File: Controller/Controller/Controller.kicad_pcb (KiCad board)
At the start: 2 copper layers, 125 parts, among them J1 Conn_01x01_Pin, J10 Conn_01x01_Pin, J11 Conn_02x05_Odd_Even, J2 Conn_01x01_Pin, J3 Conn_01x01_Pin, J4 Conn_01x01_Pin, J5 Conn_01x01_Pin, J6 Conn_01x01_Pin, J7 Conn_01x01_Pin, J8 Conn_01x01_Pin, J9 Conn_01x01_Pin, Q1 2N3906, Q2 2N5457, Q3 2N5457, U1 TL071, U2 TL072, U3 LF444, U4 TL074, U5 TL074, U6 TL072

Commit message: controller almost routed
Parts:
- added J12: Conn_01x01_Pin, Connector_Pin:Pin_D1.0mm_L10.0mm, F.Cu at (37.6, 149.9)
- added J13: Conn_01x01_Pin, Connector_Pin:Pin_D1.0mm_L10.0mm, F.Cu at (147.8, 146.6)
- C3: renamed from C24; value 100nF -> 4.7nF
- D1: renamed from D5; footprint Diode_THT:D_DO-35_SOD27_P7.62mm_Horizontal -> Diode_THT:D_T-1_P5.08mm_Horizontal
- D10, D11, D4, D6, D7: footprint Diode_THT:D_DO-35_SOD27_P7.62mm_Horizontal -> Diode_THT:D_T-1_P5.08mm_Horizontal
- D2: renamed from D1; footprint Diode_THT:D_DO-35_SOD27_P7.62mm_Horizontal -> Diode_THT:D_T-1_P5.08mm_Horizontal
- D3: renamed from D2; footprint Diode_THT:D_DO-35_SOD27_P7.62mm_Horizontal -> Diode_THT:D_T-1_P5.08mm_Horizontal
- D5: renamed from D3; footprint Diode_THT:D_DO-35_SOD27_P7.62mm_Horizontal -> Diode_THT:D_T-1_P5.08mm_Horizontal
- D8: renamed from D9; footprint Diode_THT:D_DO-35_SOD27_P7.62mm_Horizontal -> Diode_THT:D_T-1_P5.08mm_Horizontal
- D9: renamed from D8; footprint Diode_THT:D_DO-35_SOD27_P7.62mm_Horizontal -> Diode_THT:D_T-1_P5.08mm_Horizontal
- R11: renamed from R53; value 1M -> 100K
- R15: renamed from R46; value 10k -> 100k
- R6: renamed from R51; value 1M -> 300K
- R9: renamed from R52; value 1M -> 100K
- moved C17 208.0 mm to (42.7, 128.2), turned to 90 degrees
- moved C22 207.2 mm to (50.3, 144.0), turned to 90 degrees
- moved C21 186.7 mm to (63.5, 128.3), turned to 90 degrees
- moved C14 184.6 mm to (63.0, 144.0), turned to 90 degrees
- moved C16 174.7 mm to (85.1, 144.0), turned to 90 degrees
- moved C19 165.5 mm to (85.1, 128.0), turned to 90 degrees
- moved C18 154.2 mm to (105.4, 144.0), turned to 90 degrees
- moved C15 153.7 mm to (97.8, 128.2), turned to 90 degrees
- moved C4 153.1 mm to (42.2, 146.8), turned to 90 degrees
- moved C1 137.0 mm to (53.1, 139.7), turned to 90 degrees
- moved C5 130.3 mm to (60.5, 146.8)
- moved C12 129.2 mm to (120.9, 144.0), turned to 90 degrees
- moved C2 127.8 mm to (58.4, 128.3), turned to 180 degrees
- moved R5 127.5 mm to (44.5, 146.8), turned to 90 degrees
- moved C11 124.3 mm to (120.9, 128.2), turned to 90 degrees
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- renumbered C20 to C1, C19 to C10, C3 to C11, C1 to C12, C4 to C13, C2 to C14, C5 to C15, C10 to C16, C6 to C17, C11 to C18, C7 to C19, C21 to C2, C12 to C20, C8 to C21, C13 to C22, C9 to C23, C14 to C24, C15 to C25, C16 to C26, C17 to C4, C22 to C5, C25 to C6, C26 to C7, C23 to C8, C18 to C9, J11 to J1, J9 to J10, J10 to J11, J1 to J2, J2 to J3, J3 to J4, J4 to J5, J5 to J6, J6 to J7, J7 to J8, J8 to J9, Q3 to Q1, Q1 to Q3, R38 to R1, R42 to R10, R44 to R12, R45 to R13, R54 to R14, R47 to R16, R55 to R17, R49 to R18, R48 to R19, R39 to R2, R37 to R20, R35 to R21, R36 to R22, R57 to R23, R56 to R24, R59 to R25, R58 to R26, R60 to R27, R61 to R28, R1 to R29, R50 to R3, R10 to R30, R19 to R31, R2 to R32, R11 to R33, R20 to R34, R3 to R35, R12 to R36, R21 to R37, R4 to R38, R13 to R39, R40 to R4, R22 to R40, R5 to R41, R14 to R42, R23 to R43, R6 to R44, R15 to R45, R24 to R46, R7 to R47, R16 to R48, R25 to R49, R34 to R5, R8 to R50, R17 to R51, R26 to R52, R9 to R53, R18 to R54, R27 to R55, R28 to R56, R29 to R57, R30 to R58, R31 to R59, R32 to R60, R33 to R61, R41 to R7, R43 to R8, U5 to U1, U4 to U2, U2 to U3, U3 to U4, U6 to U5, U1 to U6
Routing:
- net -12V: track 6.86 -> 205.4 mm, vias 0 -> 1
- net +12V: track 6.86 -> 187.0 mm
- net TLA: track 0.00 -> 96.2 mm
- net GLA: track 0.00 -> 86.0 mm
- net Net-(Q2-S): track 0.00 -> 78.5 mm
- net ISRC: track 2.00 -> 62.0 mm
- net Net-(U1B--): track 0.00 -> 42.2 mm
- net CV2: track 0.00 -> 39.6 mm
- net Net-(D6-K): track 0.00 -> 27.9 mm
- net KBUS: track 0.00 -> 27.0 mm
- net Net-(Q3-E): track 0.00 -> 26.6 mm
- net Net-(D4-K): track 0.00 -> 25.8 mm
- net Net-(U2B-+): track 0.00 -> 22.5 mm
- net CV1: track 0.00 -> 20.3 mm
- net Net-(Q3-B): track 0.00 -> 19.7 mm
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- added copper zone on B.Cu, net GND

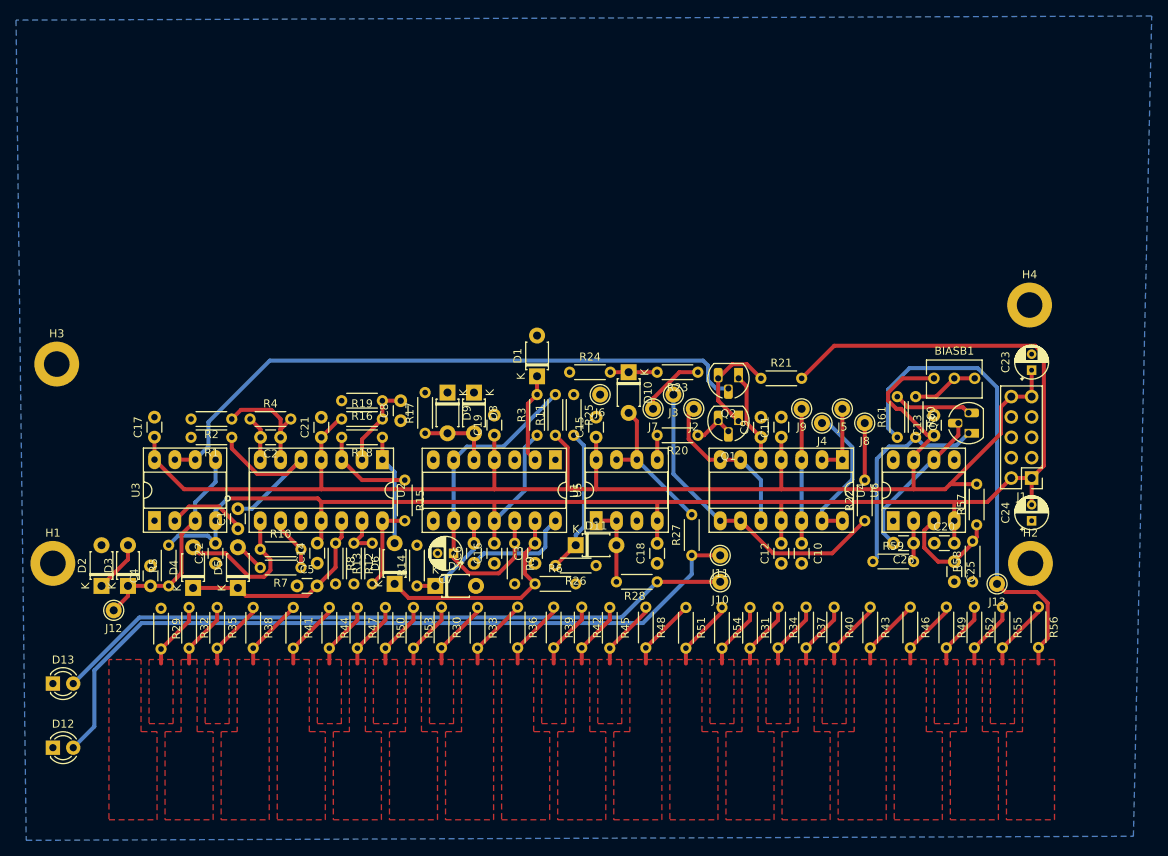
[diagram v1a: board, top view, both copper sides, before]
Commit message: controller routed
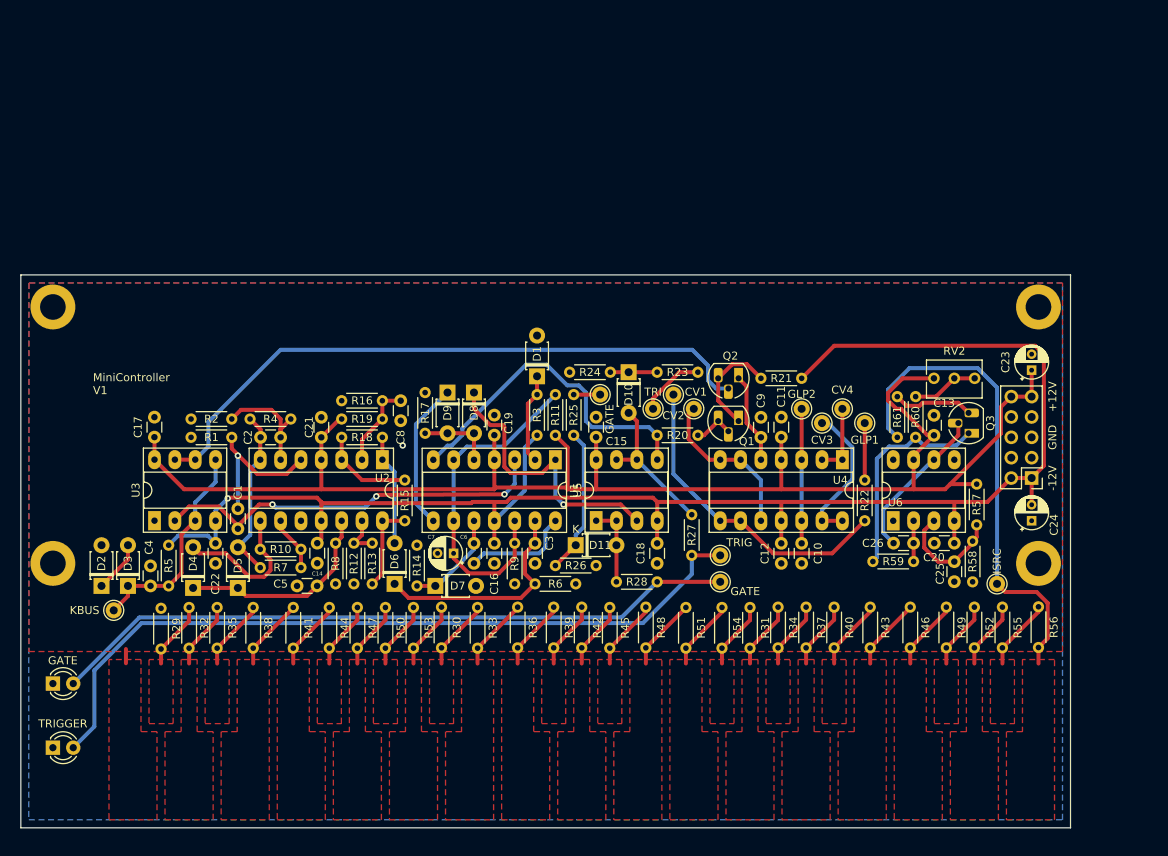
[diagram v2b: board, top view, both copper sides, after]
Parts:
- moved H3 7.14 mm to (30.0, 112.0)
- moved H4 1.13 mm to (153.0, 112.0)
- moved H2 1.00 mm to (153.0, 144.0)
- renumbered BIASB1 to RV2
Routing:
- net Net-(U1A-+): track 9.97 -> 50.4 mm, vias 0 -> 3
- net Net-(U5B-+): track 3.04 -> 42.1 mm
- net Net-(D8-K): track 0.00 -> 35.1 mm, vias 0 -> 1
- net Net-(D9-K): track 0.00 -> 18.5 mm
- net Net-(D5-A): track 9.49 -> 21.6 mm
- net Net-(U2B-+): track 22.5 -> 18.8 mm, vias 0 -> 1
- net GATE: track 0.00 -> 3.30 mm
- net GND: track 0.00 -> 1.78 mm, vias 0 -> 1
- net Net-(Q2-S): track 78.5 -> 79.6 mm
- net -12V: track 205.4 -> 206.1 mm
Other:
- board outline added: 131 x 69 mm
- board text added: "+12V"
- board text added: "-12V"
- board text added: "CV1"
- board text added: "CV2"
- board text added: "CV3"
- board text added: "CV4"
- board text added: "GATE"
- board text added: "GLP1"
- board text added: "GLP2"
- board text added: "GND"
- board text added: "ISRC"
- board text added: "KBUS"
- board text added: "MiniController V1"
- board text added: "TRI"
- board text added: "TRIG"
- board text added: "TRIGGER"

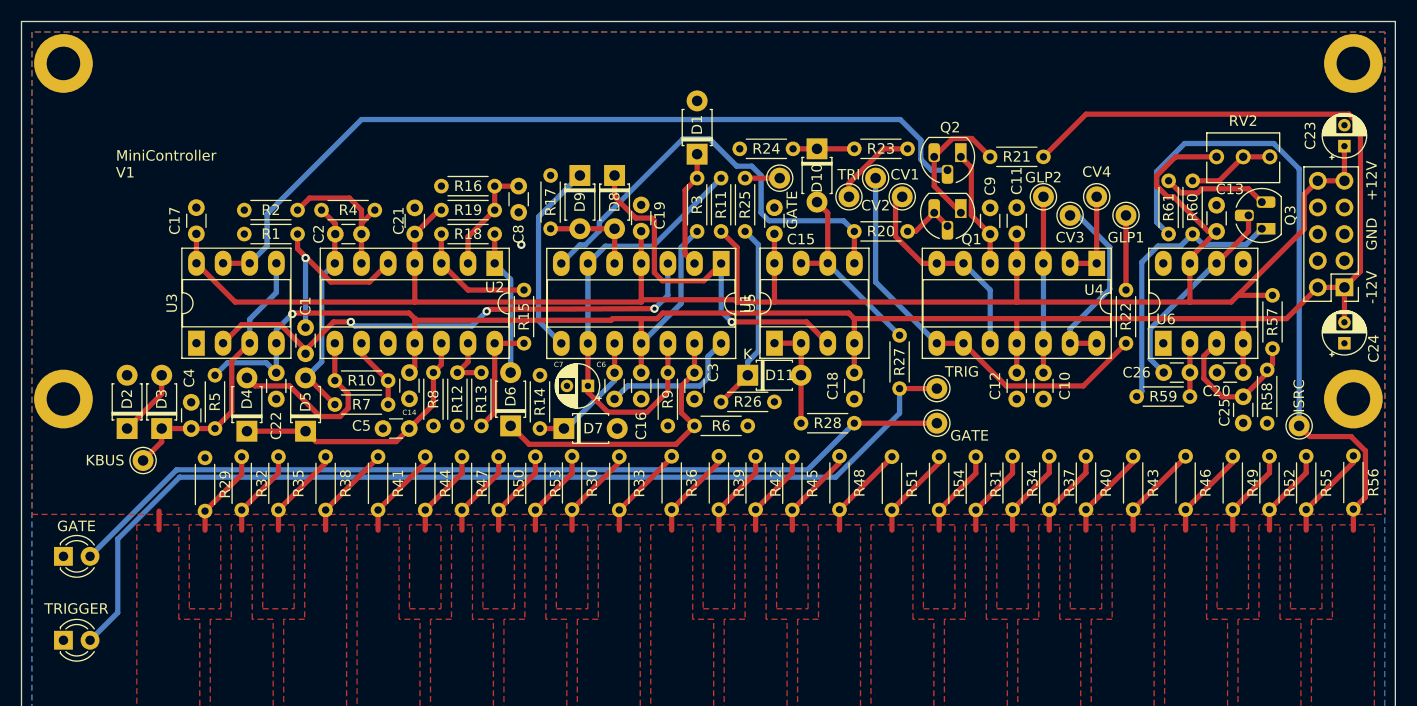
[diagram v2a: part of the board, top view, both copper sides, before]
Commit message: controller - changed resistor sizes
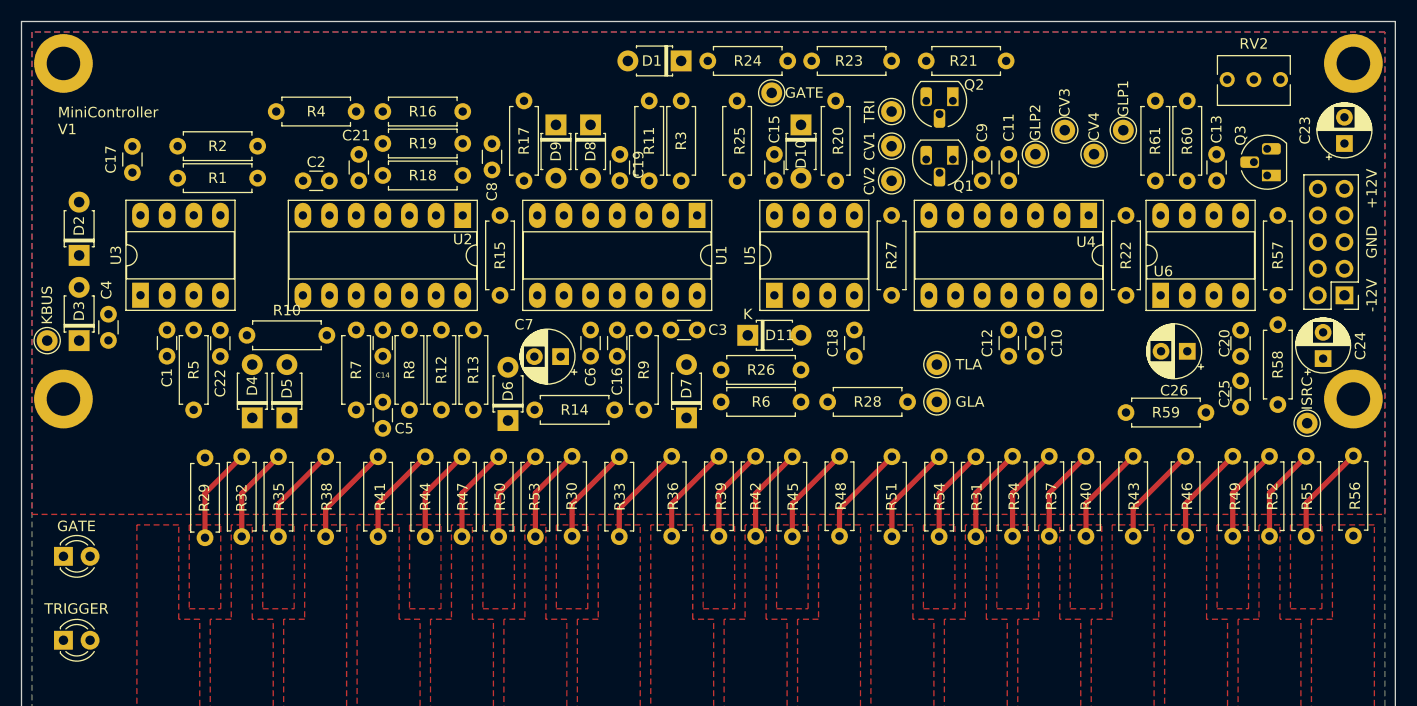
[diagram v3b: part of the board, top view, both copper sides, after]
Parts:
- C23, C24, C7: footprint Capacitor_THT:CP_Radial_D4.0mm_P2.00mm -> Capacitor_THT:CP_Radial_D5.0mm_P2.50mm
- C26: footprint Capacitor_THT:C_Disc_D3.0mm_W1.6mm_P2.50mm -> Capacitor_THT:CP_Radial_D5.0mm_P2.50mm
- R1, R10, R11, R12, R13, R14, R15, R16, R17, R18, R19, R2, R20, R21, R22, R23, R24, R25, R26, R27, R28, R29, R3, R30, R31, R32, R33, R34, R35, R36, R37, R38, R39, R4, R40, R41, R42, R43, R44, R45, R46, R47, R48, R49, R5, R50, R51, R52, R53, R54, R55, R56, R57, R58, R59, R6, R60, R61, R7, R8, R9: footprint Resistor_THT:R_Axial_DIN0204_L3.6mm_D1.6mm_P5.08mm_Horizontal -> Resistor_THT:R_Axial_DIN0207_L6.3mm_D2.5mm_P7.62mm_Horizontal
- moved D2 17.1 mm to (31.5, 130.3)
- moved J12 14.6 mm to (28.4, 138.4)
- moved R20 14.2 mm to (103.6, 115.6), turned to -90 degrees
- moved C1 13.4 mm to (39.9, 137.4), turned to -90 degrees
- moved D7 11.7 mm to (89.4, 145.8), turned to 90 degrees
- moved C4 11.5 mm to (34.3, 138.4)
- moved D3 11.5 mm to (31.5, 138.4)
- moved R21 11.0 mm to (112.3, 111.8)
- moved R4 10.3 mm to (50.3, 116.6)
- moved R5 9.62 mm to (42.4, 137.4), turned to -90 degrees
- moved R10 9.43 mm to (47.5, 137.9)
- moved R13 9.18 mm to (69.1, 137.4), turned to -90 degrees
- moved J7 9.09 mm to (109.0, 116.6)
- moved D1 9.02 mm to (88.9, 111.8), turned to 180 degrees
- moved R27 8.92 mm to (109.0, 134.1)
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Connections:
- net TRI renamed TRIG
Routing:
- net -12V: track 206.1 -> 0.00 mm, vias 1 -> 0
- net +12V: track 187.1 -> 0.00 mm
- net TLA: track 96.2 -> 0.00 mm
- net GLA: track 86.0 -> 0.00 mm
- net Net-(Q2-S): track 79.6 -> 0.00 mm
- net ISRC: track 62.0 -> 0.00 mm
- net Net-(U1A-+): track 50.4 -> 0.00 mm, vias 3 -> 0
- net Net-(U1B--): track 42.1 -> 0.00 mm
- net Net-(U5B-+): track 42.1 -> 0.00 mm
- net CV2: track 39.6 -> 0.00 mm
- net Net-(D8-K): track 35.1 -> 0.00 mm, vias 1 -> 0
- net Net-(D6-K): track 27.9 -> 0.00 mm
- net KBUS: track 27.0 -> 0.00 mm
- net Net-(Q3-E): track 26.6 -> 0.00 mm
- net Net-(D4-K): track 25.8 -> 0.00 mm
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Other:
- board text added: "GLA"
- board text added: "TLA"
- board text removed: "TRIG"

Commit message: controller routed with correct resistor sizes
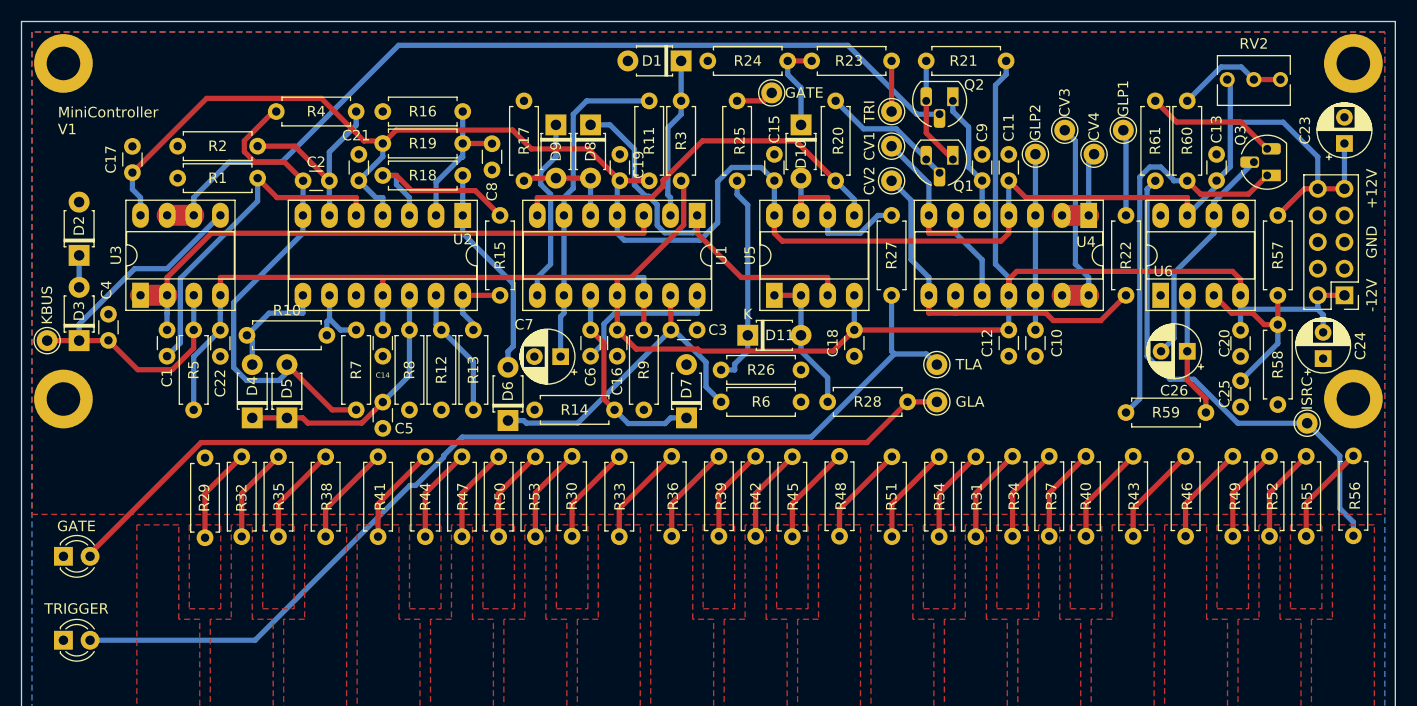
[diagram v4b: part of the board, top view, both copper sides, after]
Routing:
- net +12V: track 0.00 -> 187.8 mm
- net -12V: track 0.00 -> 186.0 mm
- net TLA: track 0.00 -> 98.3 mm
- net GLA: track 0.00 -> 87.0 mm
- net Net-(Q2-S): track 0.00 -> 84.1 mm
- net Net-(U1A-+): track 0.00 -> 56.5 mm
- net Net-(D5-A): track 0.00 -> 48.7 mm
- net ISRC: track 0.00 -> 47.5 mm
- net Net-(U1B--): track 0.00 -> 44.0 mm
- net KBUS: track 0.00 -> 40.4 mm
- net Net-(U5B-+): track 0.00 -> 38.3 mm
- net Net-(Q3-E): track 0.00 -> 37.4 mm
- net Net-(D8-K): track 0.00 -> 36.6 mm
- net CV2: track 0.00 -> 35.9 mm
- net Net-(U2B-+): track 0.00 -> 32.4 mm
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
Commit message: Controller - minor clean up
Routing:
- net Net-(D10-A): track 18.0 -> 13.6 mm
- net CV1: track 22.7 -> 19.3 mm
- net Net-(U2A-+): track 18.4 -> 15.2 mm
- net Net-(U2B-+): track 32.4 -> 31.4 mm
- net Net-(D8-K): track 36.6 -> 35.6 mm
- net GND: vias 0 -> 1
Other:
- board text added: "JLCJLCJLCJLC"

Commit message: minor cleanup
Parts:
- R1, R10, R11, R12, R13, R14, R15, R16, R17, R18, R19, R2, R20, R21, R22, R23, R24, R25, R26, R27, R28, R29, R3, R30, R31, R32, R33, R34, R35, R36, R37, R38, R39, R4, R40, R41, R42, R43, R44, R45, R46, R47, R48, R49, R5, R50, R51, R52, R53, R54, R55, R56, R57, R58, R59, R6, R60, R61, R7, R8, R9: footprint Resistor_THT:R_Axial_DIN0207_L6.3mm_D2.5mm_P7.62mm_Horizontal -> Library:R_Axial_DIN0207_L6.3mm_D2.5mm_P7.62mm_Horizontal
- moved C7 1.55 mm to (77.7, 138.4)
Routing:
- net GND: track 0.00 -> 2.96 mm
- net Net-(U1B--): track 44.0 -> 42.4 mm

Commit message: Controller - PCB cleanup
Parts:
- C26: footprint Capacitor_THT:CP_Radial_D5.0mm_P2.50mm -> Capacitor_THT:C_Disc_D3.0mm_W1.6mm_P2.50mm
- C9: footprint Capacitor_THT:C_Disc_D3.0mm_W1.6mm_P2.50mm -> Capacitor_THT:C_Radial_D8.0mm_H11.5mm_P3.50mm
- moved C9 12.5 mm to (124.5, 112.8), turned to 0 degrees
- moved J4 4.06 mm to (125.5, 122.4)
- moved J8 4.06 mm to (131.1, 122.4)
- moved D1 3.81 mm to (85.1, 111.8)
- moved C26 2.45 mm to (137.2, 137.0)
- moved C15 0.51 mm to (97.3, 123.2)
- moved D6 0.25 mm to (72.1, 146.1)
- moved J9 0.25 mm to (122.9, 120.7)
- moved J12 0.25 mm to (28.2, 138.4)
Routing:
- net -12V: track 186.0 -> 200.7 mm
- net Net-(Q2-D): track 12.1 -> 22.9 mm
- net GLP1: track 8.23 -> 4.17 mm
- net CV3: track 19.2 -> 15.2 mm
- net Net-(Q3-B): track 21.7 -> 19.3 mm
- net Net-(D1-K): track 15.4 -> 16.9 mm
- net Net-(U5B-+): track 38.3 -> 39.7 mm
- net Net-(D4-K): track 24.7 -> 25.8 mm
- net Net-(D7-K): track 19.5 -> 20.5 mm
- net GLP2: track 16.8 -> 17.6 mm
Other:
- board text added: "MiniController V2"
- board text removed: "MiniController V1"

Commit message: Controller - incomplete fixes
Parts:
- added K1: ~, Library:Keyboard 5 keys, F.Cu at (37.1, 155.9)
- added K3: ~, Library:Keyboard 5 keys, F.Cu at (85.8, 155.9)
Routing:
- removed copper zone on F.Cu, net K13
- removed copper zone on F.Cu, net K14
- removed copper zone on F.Cu, net K15
- removed copper zone on F.Cu, net K16
- removed copper zone on F.Cu, net K17
- removed copper zone on F.Cu, net K2
- removed copper zone on F.Cu, net K3
- removed copper zone on F.Cu, net K4
- removed copper zone on F.Cu, net K5
